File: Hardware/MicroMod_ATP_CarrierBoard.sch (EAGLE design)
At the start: 70 parts, among them J19 QWIIC_RIGHT_ANGLE, J2 JTAG, J20 QWIIC_RIGHT_ANGLE, J21 1X04_SMD_STRAIGHT_COMBO, J4 USB_A_SMT_FEMALE, J6 MICROMOD-2222-C, J8 1X04_SMD_STRAIGHT_COMBO, U5 AP7361C-33

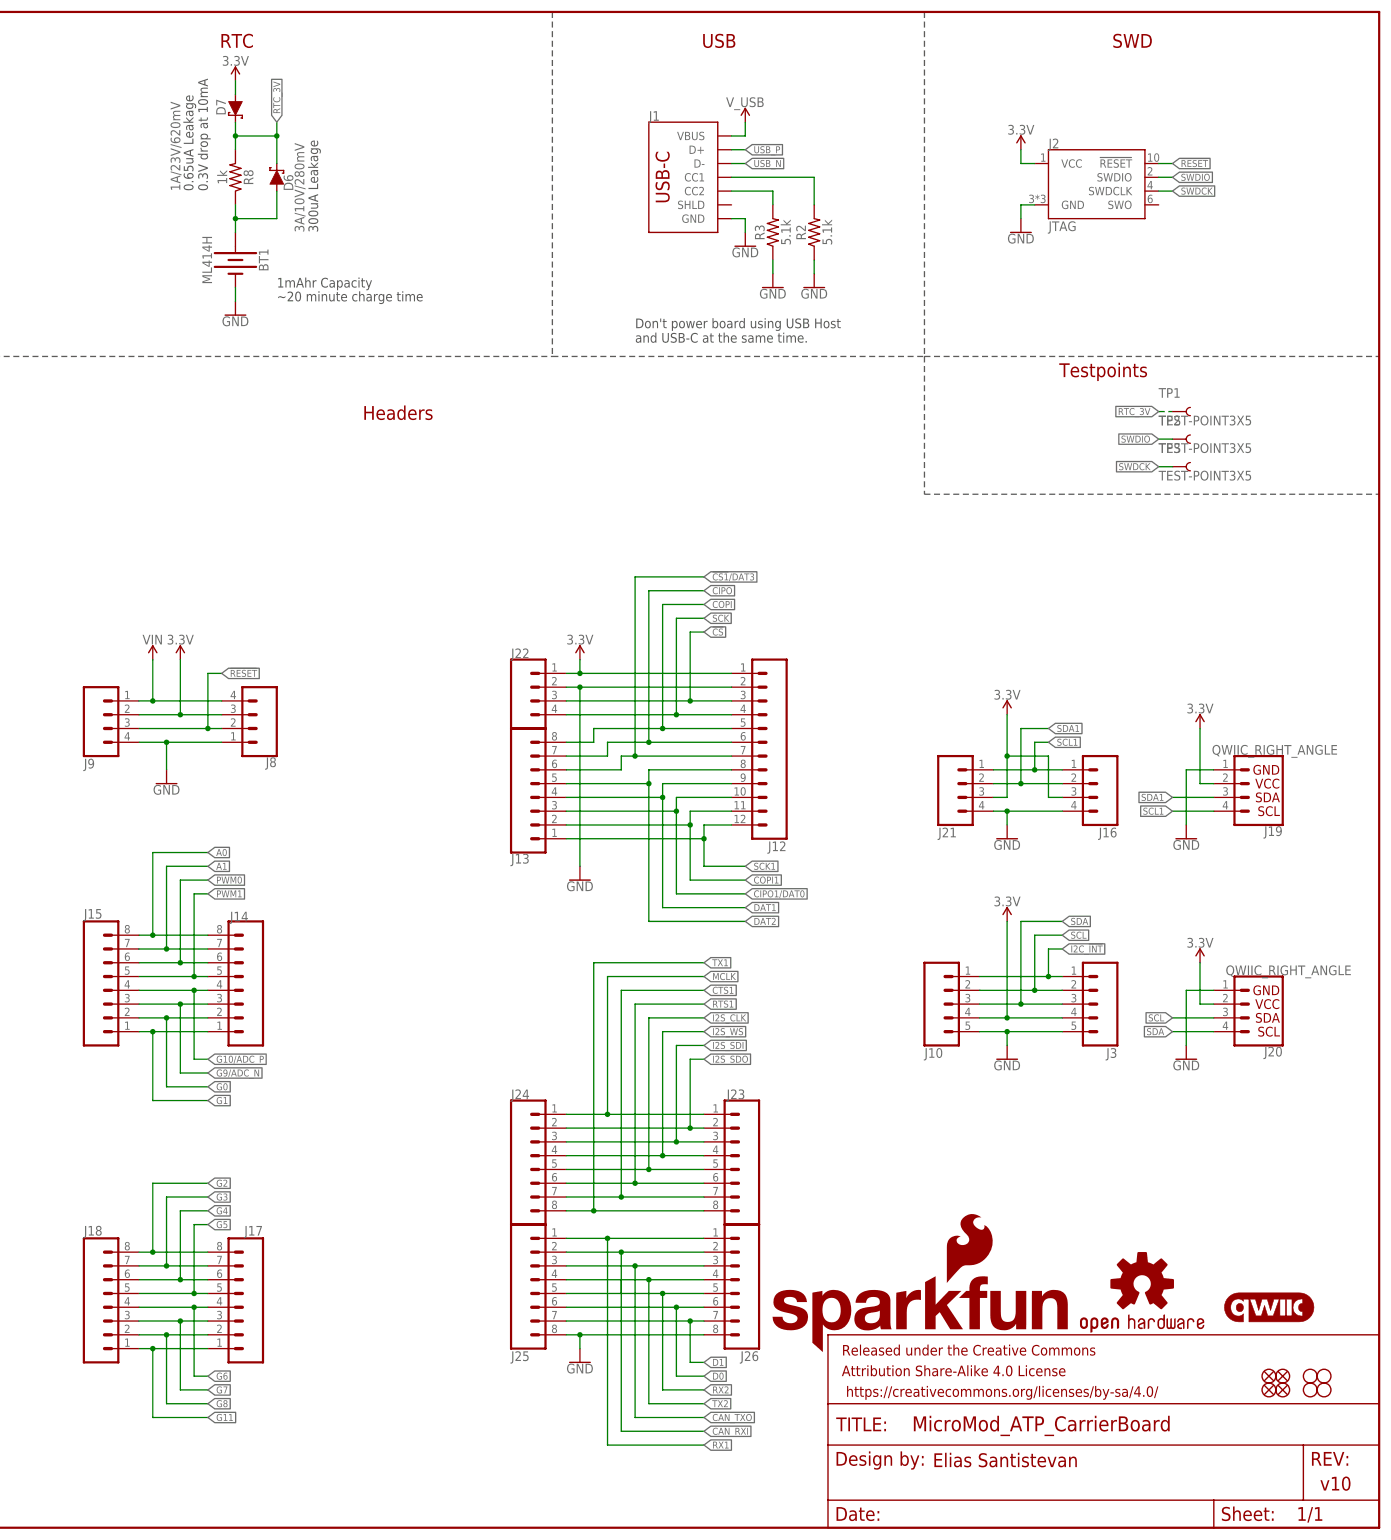
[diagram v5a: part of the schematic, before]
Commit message: Fixes some proportional font, swaps SDA and SCL on I2C qwiic connector, adds additional qwiic logo
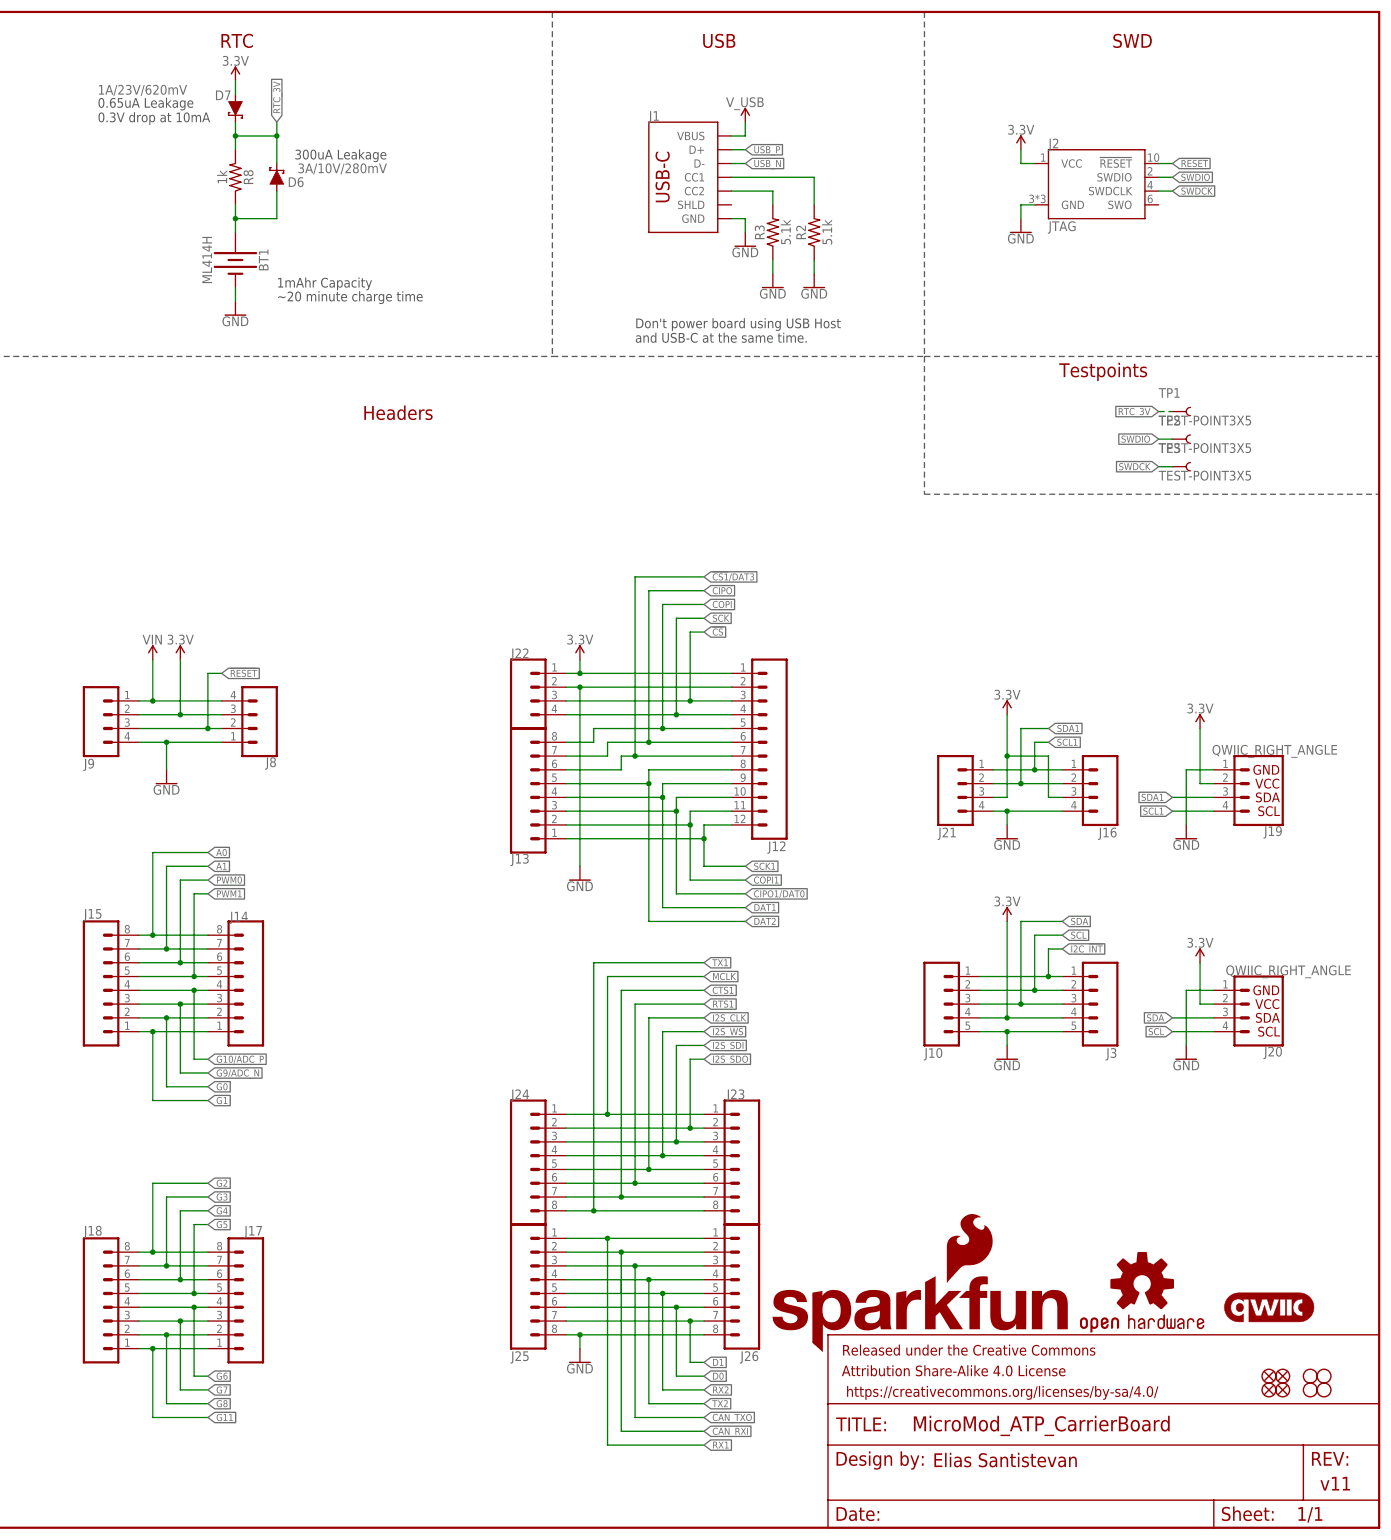
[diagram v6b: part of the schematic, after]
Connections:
- net SCL: now also J20.4; no longer J20.3
- net SDA: now also J20.3; no longer J20.4
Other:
- note added: "v11"
- note removed: "v10"
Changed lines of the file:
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@@
 <sheet>
 <plain>
-<text x="236.22" y="238.76" size="1.778" layer="97" rot="R90">300uA Leakage</text>
-<text x="215.9" y="246.38" size="1.778" layer="97" rot="R90">0.65uA Leakage
+<text x="248.92" y="254" size="1.778" layer="97" font="vector" rot="R180">300uA Leakage</text>
+<text x="195.58" y="259.08" size="1.778" layer="97" font="vector">0.65uA Leakage
 0.3V drop at 10mA</text>
-<text x="228.6" y="226.06" size="1.778" layer="97">~20 minute charge time</text>
-<text x="228.6" y="228.6" size="1.778" layer="97">1mAhr Capacity</text>
+<text x="228.6" y="226.06" size="1.778" layer="97" font="vector">~20 minute charge time</text>
+<text x="228.6" y="228.6" size="1.778" layer="97" font="vector">1mAhr Capacity</text>
 <text x="121.666" y="268.986" size="1.778" layer="97" font="vector">Take care when closing this jumper,
  it removes the 6V/2A fuse. </text>
@@
 <text x="43.18" y="226.06" size="2.54" layer="94" font="vector" align="center">USB Host</text>
 <text x="137.16" y="53.34" size="2.54" layer="94" font="vector" align="center">Buttons</text>
-<text x="420.878" y="6.858" size="2.54" layer="94" font="vector">v10</text>
+<text x="420.878" y="6.858" size="2.54" layer="94" font="vector">v11</text>
 <wire x1="167.64" y1="60.96" x2="109.22" y2="60.96" width="0.2032" layer="97" style="longdash"/>
 <wire x1="109.22" y1="60.96" x2="109.22" y2="0" width="0.2032" layer="97" style="longdash"/>
@@
 </instance>
 <instance part="D6" gate="G$1" x="228.6" y="248.92" smashed="yes" rot="R90">
-<attribute name="NAME" x="231.648" y="246.38" size="1.778" layer="95" font="vector" rot="R90"/>
-<attribute name="VALUE" x="233.68" y="238.76" size="1.778" layer="96" font="vector" rot="MR90" align="top-left"/>
+<attribute name="NAME" x="233.68" y="248.92" size="1.778" layer="95" font="vector" rot="R180"/>
+<attribute name="VALUE" x="248.92" y="251.46" size="1.778" layer="96" font="vector" rot="MR0" align="top-left"/>
 </instance>
 <instance part="R8" gate="G$1" x="220.98" y="248.92" smashed="yes" rot="MR90">
@@
 </instance>
 <instance part="D7" gate="G$1" x="220.98" y="261.62" smashed="yes" rot="R270">
-<attribute name="NAME" x="217.424" y="263.398" size="1.778" layer="95" font="vector" rot="R270"/>
-<attribute name="VALUE" x="210.82" y="246.38" size="1.778" layer="96" font="vector" rot="MR90" align="top-left"/>
+<attribute name="NAME" x="217.17" y="263.144" size="1.778" layer="95" font="vector"/>
+<attribute name="VALUE" x="195.58" y="264.16" size="1.778" layer="96" font="vector" rot="MR180" align="top-left"/>
 </instance>
 <instance part="SUPPLY1" gate="G$1" x="30.48" y="134.62" smashed="yes">
@@
 </segment>
 <segment>
-<wire x1="401.32" y1="93.98" x2="393.7" y2="93.98" width="0.1524" layer="91"/>
-<label x="393.7" y="93.98" size="1.27" layer="95" rot="R180" xref="yes"/>
-<pinref part="J20" gate="G$1" pin="3"/>
+<wire x1="401.32" y1="91.44" x2="393.7" y2="91.44" width="0.1524" layer="91"/>
+<label x="393.7" y="91.44" size="1.27" layer="95" rot="R180" xref="yes"/>
+<pinref part="J20" gate="G$1" pin="4"/>
 </segment>
 </net>
@@
 </segment>
 <segment>
-<wire x1="401.32" y1="91.44" x2="393.7" y2="91.44" width="0.1524" layer="91"/>
-<label x="393.7" y="91.44" size="1.27" layer="95" rot="R180" xref="yes"/>
-<pinref part="J20" gate="G$1" pin="4"/>
-</segment>
-</net>
+<wire x1="401.32" y1="93.98" x2="393.7" y2="93.98" width="0.1524" layer="91"/>
+<label x="393.7" y="93.98" size="1.27" layer="95" rot="R180" xref="yes"/>
+<pinref part="J20" gate="G$1" pin="3"/>
+</segment>
+</net>
